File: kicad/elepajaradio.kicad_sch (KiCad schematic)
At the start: 29 parts, among them J1 SPI, J2 UART, J3 vdd_gnd, J4 reset, J5 OLED, SW1 RotaryEncoder, SW2 SW_Push, SW3 SW_Push, U1 MAX2606, U3 ATmega328PB-A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

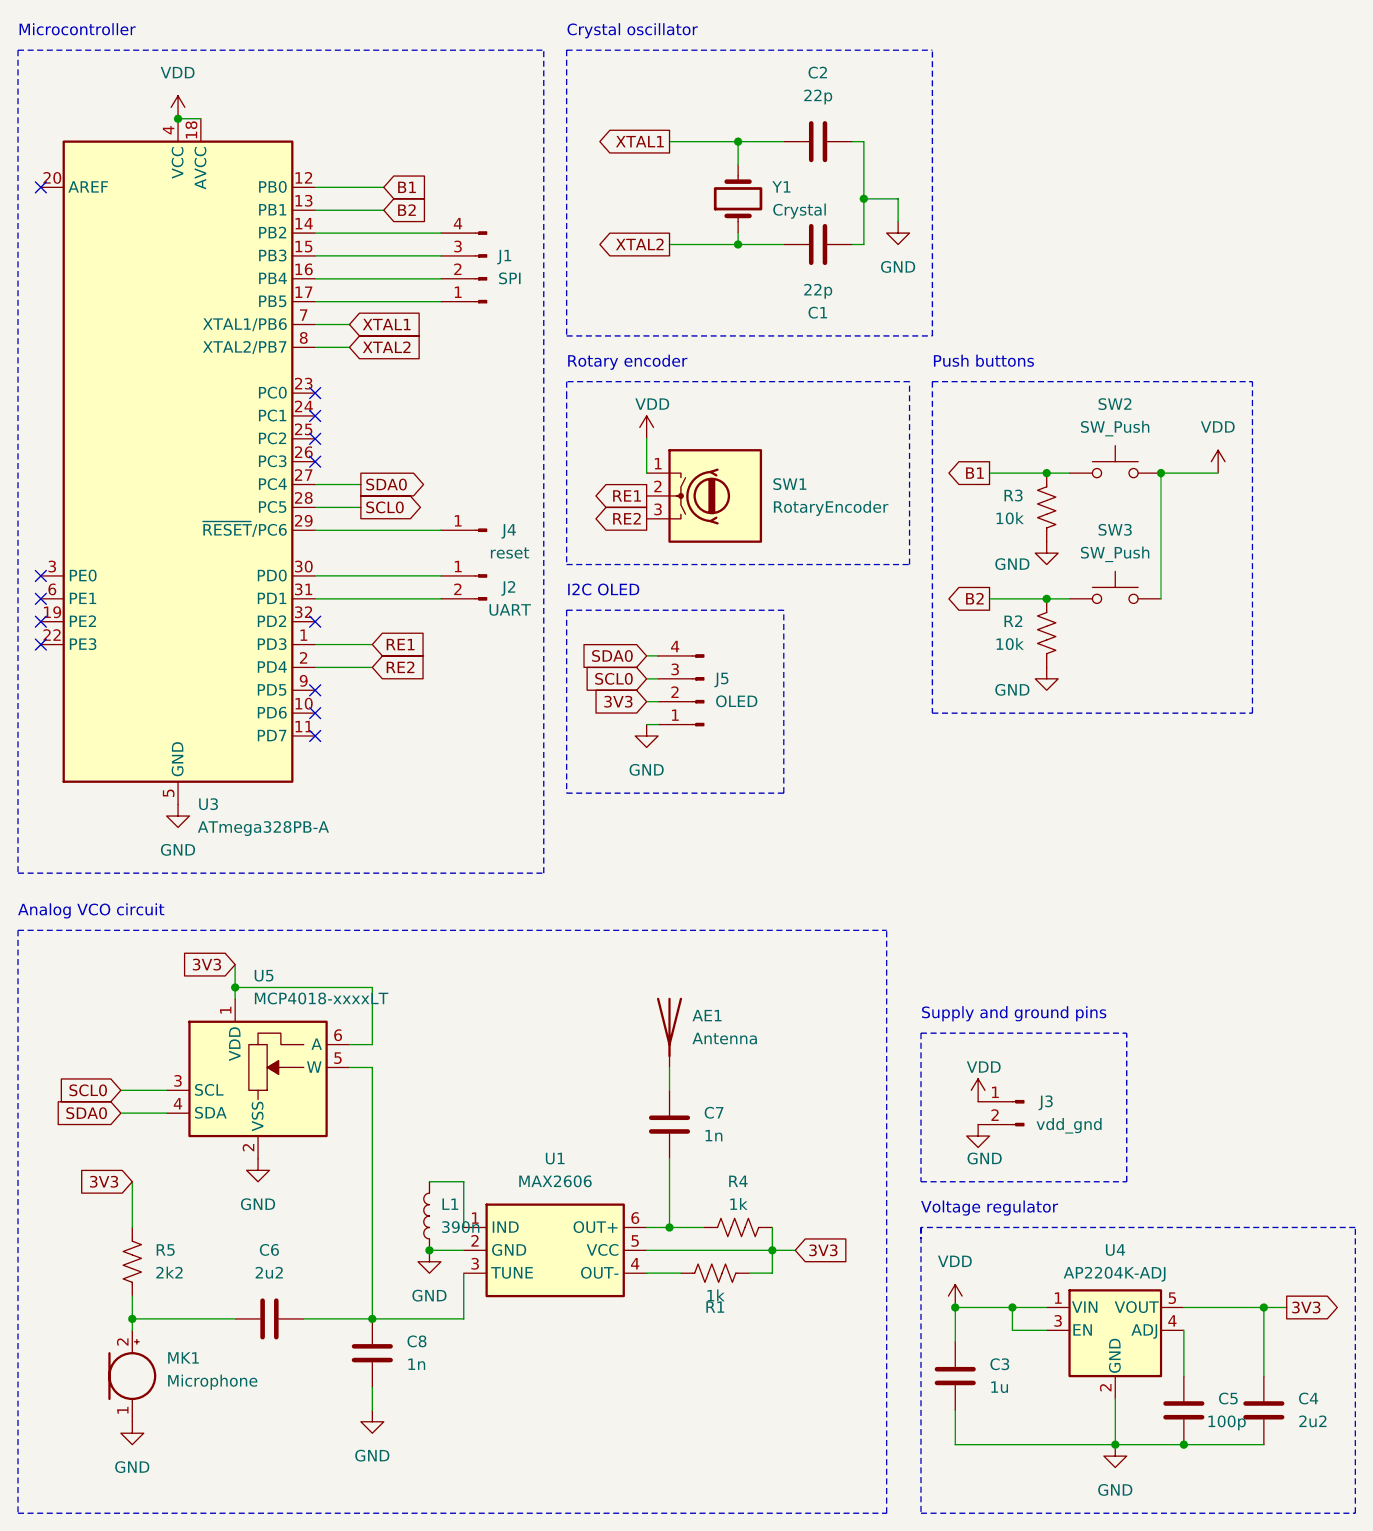
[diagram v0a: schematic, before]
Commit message: pull-up resistors and diode added
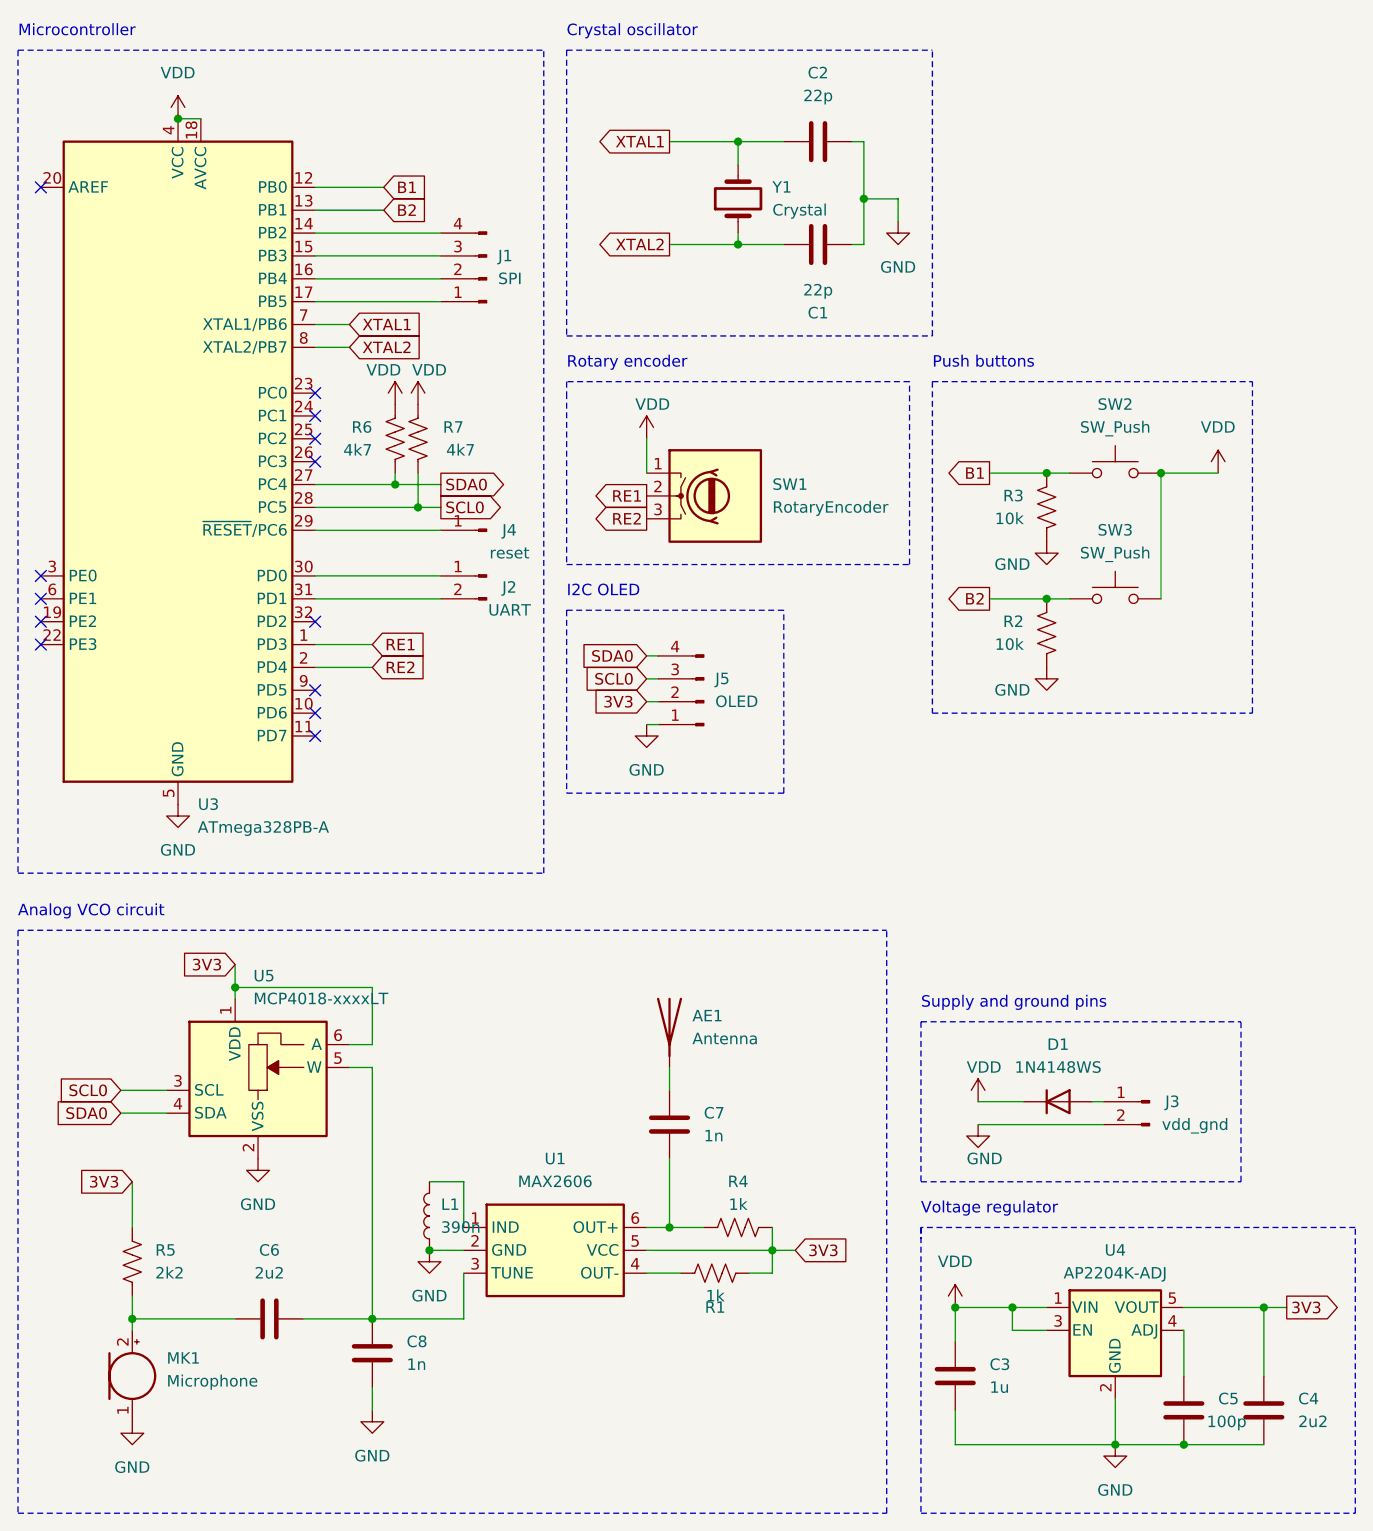
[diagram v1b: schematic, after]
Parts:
- added D1: 1N4148WS, Diode_SMD:D_SOD-323, symbol Diode:1N4148WS
- added R6, R7: 4k7, Resistor_SMD:R_0603_1608Metric, symbol Device:R_US
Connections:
- net SCL0: now also R7.1
- net SDA0: now also R6.1
- net VDD: now also D1.1 (K), R6.2, R7.2; no longer J3.1 (Pin_1)
- new net: D1.2 (A), J3.1 (Pin_1)
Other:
- moved on the sheet: J3
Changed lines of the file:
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@@
   (junction (at 34.29 24.13) (diameter 0) (color 0 0 0 0)
   )
+  (junction (at 60.96 67.31) (diameter 0) (color 0 0 0 0)
+  )
   (junction (at 96.52 38.1) (diameter 0) (color 0 0 0 0)
   )
@@
   )
   (junction (at 88.9 147.32) (diameter 0) (color 0 0 0 0)
+  )
+  (junction (at 58.42 64.77) (diameter 0) (color 0 0 0 0)
   )
   (junction (at 130.81 77.47) (diameter 0) (color 0 0 0 0)
@@
     (stroke (width 0) (type default))
   )
+  (wire (pts (xy 58.42 64.77) (xy 49.53 64.77))
+    (stroke (width 0) (type default))
+  )
   (wire (pts (xy 130.81 156.21) (xy 127 156.21))
     (stroke (width 0) (type default))
@@
     (stroke (width 0) (type default))
   )
+  (wire (pts (xy 137.16 135.89) (xy 123.19 135.89))
+    (stroke (width 0) (type default))
+  )
   (wire (pts (xy 110.49 26.67) (xy 110.49 33.02))
     (stroke (width 0) (type default))
@@
     (stroke (width 0) (type default))
   )
-  (polyline (pts (xy 116.84 142.24) (xy 139.7 142.24))
+  (wire (pts (xy 60.96 63.5) (xy 60.96 67.31))
+    (stroke (width 0) (type default))
+  )
+  (polyline (pts (xy 116.84 142.24) (xy 152.4 142.24))
     (stroke (width 0) (type dash))
   )
@@
     (stroke (width 0) (type default))
   )
-  (polyline (pts (xy 116.84 125.73) (xy 139.7 125.73))
+  (polyline (pts (xy 116.84 124.46) (xy 152.4 124.46))
     (stroke (width 0) (type dash))
   )
@@
     (stroke (width 0) (type default))
   )
+  (wire (pts (xy 60.96 67.31) (xy 49.53 67.31))
+    (stroke (width 0) (type default))
+  )
   (wire (pts (xy 96.52 38.1) (xy 101.6 38.1))
     (stroke (width 0) (type default))
@@
     (stroke (width 0) (type default))
   )
+  (wire (pts (xy 58.42 63.5) (xy 58.42 64.77))
+    (stroke (width 0) (type default))
+  )
   (wire (pts (xy 110.49 33.02) (xy 110.49 38.1))
     (stroke (width 0) (type default))
   )
-  (wire (pts (xy 54.61 64.77) (xy 49.53 64.77))
+  (wire (pts (xy 63.5 64.77) (xy 58.42 64.77))
     (stroke (width 0) (type default))
   )
@@
     (stroke (width 0) (type default))
   )
-  (wire (pts (xy 54.61 67.31) (xy 49.53 67.31))
+  (wire (pts (xy 63.5 67.31) (xy 60.96 67.31))
     (stroke (width 0) (type default))
   )
@@
     (stroke (width 0) (type default))
   )
-  (polyline (pts (xy 116.84 125.73) (xy 116.84 142.24))
-    (stroke (width 0) (type dash))
+  (polyline (pts (xy 116.84 124.46) (xy 116.84 142.24))
+    (stroke (width 0) (type dash))
+  )
+  (wire (pts (xy 137.16 133.35) (xy 135.89 133.35))
+    (stroke (width 0) (type default))
   )
   (wire (pts (xy 48.26 157.48) (xy 55.88 157.48))
@@
     (stroke (width 0) (type dash))
   )
+  (wire (pts (xy 128.27 133.35) (xy 123.19 133.35))
+    (stroke (width 0) (type default))
+  )
   (polyline (pts (xy 77.47 16.51) (xy 118.11 16.51))
     (stroke (width 0) (type dash))
@@
     (stroke (width 0) (type default))
   )
-  (polyline (pts (xy 139.7 142.24) (xy 139.7 125.73))
+  (polyline (pts (xy 152.4 142.24) (xy 152.4 124.46))
     (stroke (width 0) (type dash))
   )
@@
     (effects (font (size 1.27 1.27)) (justify left bottom))
   )
-  (text "Supply and ground pins" (at 116.84 124.46 0)
+  (text "Supply and ground pins" (at 116.84 123.19 0)
     (effects (font (size 1.27 1.27)) (justify left bottom))
   )
@@
     )
   )
-  (global_label "SDA0" (shape output) (at 54.61 64.77 0) (fields_autoplaced)
+  (global_label "SDA0" (shape output) (at 63.5 64.77 0) (fields_autoplaced)
     (effects (font (size 1.27 1.27)) (justify left))
-    (property "Intersheetrefs" "${INTERSHEET_REFS}" (at 62.3728 64.77 0)
+    (property "Intersheetrefs" "${INTERSHEET_REFS}" (at 71.2628 64.77 0)
       (effects (font (size 1.27 1.27)) (justify left) hide)
     )
@@
     )
   )
-  (global_label "SCL0" (shape output) (at 54.61 67.31 0) (fields_autoplaced)
+  (global_label "SCL0" (shape output) (at 63.5 67.31 0) (fields_autoplaced)
     (effects (font (size 1.27 1.27)) (justify left))
-    (property "Intersheetrefs" "${INTERSHEET_REFS}" (at 62.3123 67.31 0)
+    (property "Intersheetrefs" "${INTERSHEET_REFS}" (at 71.2023 67.31 0)
       (effects (font (size 1.27 1.27)) (justify left) hide)
     )
@@
     )
   )
+  (symbol (lib_id "Diode:1N4148WS") (at 132.08 133.35 0) (unit 1)
+    (in_bom yes) (on_board yes) (dnp no) (fields_autoplaced)
+    (property "Reference" "D1" (at 132.08 127 0)
+      (effects (font (size 1.27 1.27)))
+    )
+    (property "Value" "1N4148WS" (at 132.08 129.54 0)
+      (effects (font (size 1.27 1.27)))
+    )
+    (property "Footprint" "Diode_SMD:D_SOD-323" (at 132.08 137.795 0)
+      (effects (font (size 1.27 1.27)) hide)
+    )
+    (property "Datasheet" "https://www.vishay.com/docs/85751/1n4148ws.pdf" (at 132.08 133.35 0)
+      (effects (font (size 1.27 1.27)) hide)
+    )
+    (property "Sim.Device" "D" (at 132.08 133.35 0)
+      (effects (font (size 1.27 1.27)) hide)
+    )
+    (property "Sim.Pins" "1=K 2=A" (at 132.08 133.35 0)
+      (effects (font (size 1.27 1.27)) hide)
+    )
+    (pin "2")
+    (pin "1")
+    (instances
+      (project "elepajaradio"
+        (path "/be645d0f-8568-47a0-a152-e3ddd33563eb"
+          (reference "D1") (unit 1)
+        )
+      )
+    )
+  )
   (symbol (lib_id "power:GND") (at 130.81 85.09 0) (unit 1)
     (in_bom yes) (on_board yes) (dnp no)
@@
     )
   )
-  (symbol (lib_id "Connector:Conn_01x02_Pin") (at 128.27 133.35 0) (mirror y) (unit 1)
+  (symbol (lib_id "Connector:Conn_01x02_Pin") (at 142.24 133.35 0) (mirror y) (unit 1)
     (in_bom yes) (on_board yes) (dnp no)
-    (property "Reference" "J3" (at 130.81 133.35 0)
-      (effects (font (size 1.27 1.27)))
-    )
-    (property "Value" "vdd_gnd" (at 133.35 135.89 0)
-      (effects (font (size 1.27 1.27)))
-    )
-    (property "Footprint" "Connector_PinHeader_2.54mm:PinHeader_1x02_P2.54mm_Vertical" (at 128.27 133.35 0)
-      (effects (font (size 1.27 1.27)) hide)
-    )
-    (property "Datasheet" "~" (at 128.27 133.35 0)
+    (property "Reference" "J3" (at 144.78 133.35 0)
+      (effects (font (size 1.27 1.27)))
+    )
+    (property "Value" "vdd_gnd" (at 147.32 135.89 0)
+      (effects (font (size 1.27 1.27)))
+    )
+    (property "Footprint" "Connector_PinHeader_2.54mm:PinHeader_1x02_P2.54mm_Vertical" (at 142.24 133.35 0)
+      (effects (font (size 1.27 1.27)) hide)
+    )
+    (property "Datasheet" "~" (at 142.24 133.35 0)
       (effects (font (size 1.27 1.27)) hide)
     )
@@
         (path "/be645d0f-8568-47a0-a152-e3ddd33563eb"
           (reference "J2") (unit 1)
+        )
+      )
+    )
+  )
+  (symbol (lib_id "Device:R_US") (at 60.96 59.69 0) (mirror x) (unit 1)
+    (in_bom yes) (on_board yes) (dnp no)
+    (property "Reference" "R7" (at 66.04 58.4199 0)
+      (effects (font (size 1.27 1.27)) (justify right))
+    )
+    (property "Value" "4k7" (at 67.31 60.96 0)
+      (effects (font (size 1.27 1.27)) (justify right))
+    )
+    (property "Footprint" "Resistor_SMD:R_0603_1608Metric" (at 61.976 59.436 90)
+      (effects (font (size 1.27 1.27)) hide)
+    )
+    (property "Datasheet" "~" (at 60.96 59.69 0)
+      (effects (font (size 1.27 1.27)) hide)
+    )
+    (pin "1")
+    (pin "2")
+    (instances
+      (project "elepajaradio"
+        (path "/be645d0f-8568-47a0-a152-e3ddd33563eb"
+          (reference "R7") (unit 1)
         )
       )
@@
     )
   )
+  (symbol (lib_id "Device:R_US") (at 58.42 59.69 0) (mirror x) (unit 1)
+    (in_bom yes) (on_board yes) (dnp no)
+    (property "Reference" "R6" (at 55.88 58.4199 0)
+      (effects (font (size 1.27 1.27)) (justify right))
+    )
+    (property "Value" "4k7" (at 55.88 60.9599 0)
+      (effects (font (size 1.27 1.27)) (justify right))
+    )
+    (property "Footprint" "Resistor_SMD:R_0603_1608Metric" (at 59.436 59.436 90)
+      (effects (font (size 1.27 1.27)) hide)
+    )
+    (property "Datasheet" "~" (at 58.42 59.69 0)
+      (effects (font (size 1.27 1.27)) hide)
+    )
+    (pin "1")
+    (pin "2")
+    (instances
+      (project "elepajaradio"
+        (path "/be645d0f-8568-47a0-a152-e3ddd33563eb"
+          (reference "R6") (unit 1)
+        )
+      )
+    )
+  )
   (symbol (lib_id "power:GND") (at 55.88 167.64 0) (unit 1)
     (in_bom yes) (on_board yes) (dnp no) (fields_autoplaced)
@@
         (path "/be645d0f-8568-47a0-a152-e3ddd33563eb"
           (reference "#PWR0104") (unit 1)
+        )
+      )
+    )
+  )
+  (symbol (lib_id "power:VDD") (at 58.42 55.88 0) (unit 1)
+    (in_bom yes) (on_board yes) (dnp no)
+    (property "Reference" "#PWR08" (at 58.42 59.69 0)
+      (effects (font (size 1.27 1.27)) hide)
+    )
+    (property "Value" "VDD" (at 57.15 52.07 0)
+      (effects (font (size 1.27 1.27)))
+    )
+    (property "Footprint" "" (at 58.42 55.88 0)
+      (effects (font (size 1.27 1.27)) hide)
+    )
+    (property "Datasheet" "" (at 58.42 55.88 0)
+      (effects (font (size 1.27 1.27)) hide)
+    )
+    (pin "1")
+    (instances
+      (project "elepajaradio"
+        (path "/be645d0f-8568-47a0-a152-e3ddd33563eb"
+          (reference "#PWR08") (unit 1)
         )
       )
@@
         )
       )
+    )
+  )
+  (symbol (lib_id "power:VDD") (at 60.96 55.88 0) (unit 1)
+    (in_bom yes) (on_board yes) (dnp no)
+    (property "Reference" "#PWR09" (at 60.96 59.69 0)
+      (effects (font (size 1.27 1.27)) hide)
+    )
+    (property "Value" "VDD" (at 62.23 52.07 0)
+      (effects (font (size 1.27 1.27)))
+    )
+    (property "Footprint" "" (at 60.96 55.88 0)
+      (effects (font (size 1.27 1.27)) hide)
+    )
+    (property "Datasheet" "" (at 60.96 55.88 0)
+      (effects (font (size 1.27 1.27)) hide)
+    )
+    (pin "1")
+    (instances
+      (project "elepajaradio"
+        (path "/be645d0f-8568-47a0-a152-e3ddd33563eb"
+          (reference "#PWR09") (unit 1)
+        )
+      )
